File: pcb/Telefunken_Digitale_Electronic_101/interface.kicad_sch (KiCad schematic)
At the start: 11 parts, among them J1 Conn_01x02_MountingPin, J2 Conn_01x02_MountingPin, J3 Conn_01x04_MountingPin

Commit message: TFK: sch - i2c resistors not populate, logo; pcb - spaced tracks, stitching vias, logo
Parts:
- added LF1: (no value), RadioWecker:LEAF, symbol RadioWecker:LEAF
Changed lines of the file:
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@@
+	)
+	(symbol
+		(lib_id "RadioWecker:LEAF")
+		(at 58.42 135.89 0)
+		(unit 1)
+		(body_style 1)
+		(exclude_from_sim no)
+		(in_bom yes)
+		(on_board yes)
+		(in_pos_files yes)
+		(dnp no)
+		(fields_autoplaced yes)
+		(property "Reference" "LF1"
+			(at 62.23 133.6674 0)
+			(show_name no)
+			(do_not_autoplace no)
+			(effects
+				(font
+					(size 1.27 1.27)
+				)
+				(justify left)
+			)
+		)
+		(property "Value" ""
+			(at 58.42 135.89 0)
+			(hide yes)
+			(show_name no)
+			(do_not_autoplace no)
+			(effects
+				(font
+					(size 1.27 1.27)
+				)
+			)
+		)
+		(property "Footprint" "RadioWecker:LEAF"
+			(at 58.674 139.192 0)
+			(hide yes)
+			(show_name no)
+			(do_not_autoplace no)
+			(effects
+				(font
+					(size 1.27 1.27)
+				)
+			)
+		)
+		(property "Datasheet" ""
+			(at 58.42 135.89 0)
+			(hide yes)
+			(show_name no)
+			(do_not_autoplace no)
+			(effects
+				(font
+					(size 1.27 1.27)
+				)
+			)
+		)
+		(property "Description" ""
+			(at 58.42 135.89 0)
+			(hide yes)
+			(show_name no)
+			(do_not_autoplace no)
+			(effects
+				(font
+					(size 1.27 1.27)
+				)
+			)
+		)
+		(instances
+			(project "Telefunken_Digitale_Electronic_101"
+				(path "/df1af5ff-c8b9-4769-9610-ead9e11e7e65/75a1a5d9-cb48-4e12-a237-e00fbc51bad9"
+					(reference "LF1")
+					(unit 1)
+				)
+			)
+		)
 	)
 	(symbol

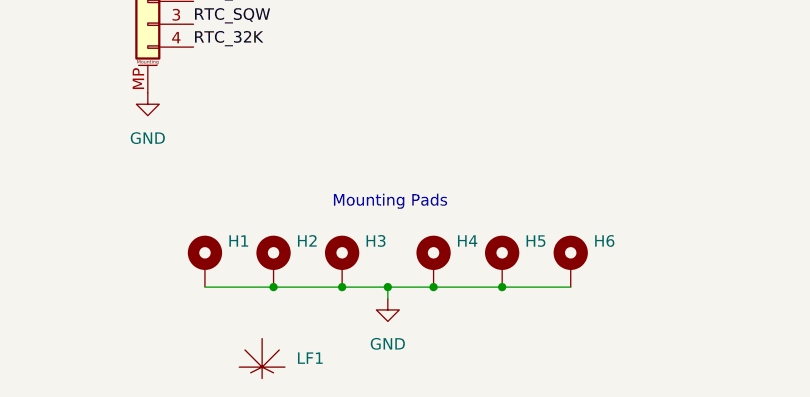
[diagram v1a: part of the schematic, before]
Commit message: PCBs: updated logo; added I2C resistors to I2C (core pcb)
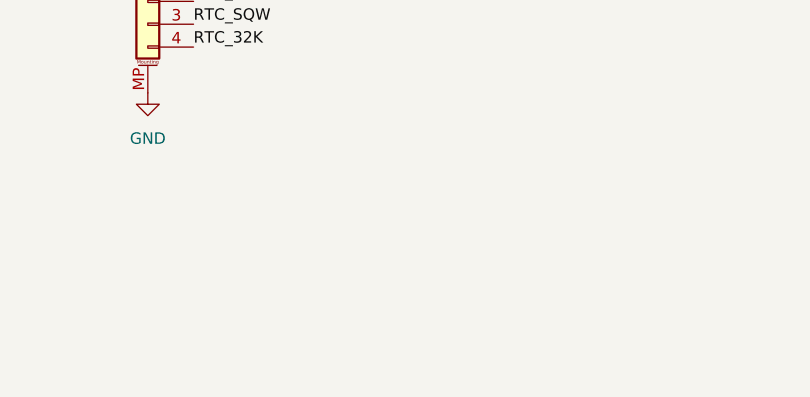
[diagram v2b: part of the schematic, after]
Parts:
- removed H1, H2, H3, H4, H5, H6: MountingHole_Pad_MP, RadioWecker:BOARD_TO_BOARD_PAD_SMD, symbol Mechanical:MountingHole_Pad_MP
- removed LF1: (no value), RadioWecker:LEAF, symbol RadioWecker:LEAF
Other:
- note removed: "Mounting Pads"
